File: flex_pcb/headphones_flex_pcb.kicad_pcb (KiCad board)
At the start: 2 copper layers, 41.7 x 25.7 mm, 15 parts, among them J1 LIGHTING_JACK, J2 CONN_01X01, J3 BOTTOM_FLEX_LIGHTNING, J5 LIGHTNING_HEADPHONE_ADAPTER, J7 IPHONE_HEADPHONE_JACK, U1 SN74LVC1G123, U2 SN74LVC1G123, U3 NC7S32-micropak6, U4 ADG774A-LFCSP

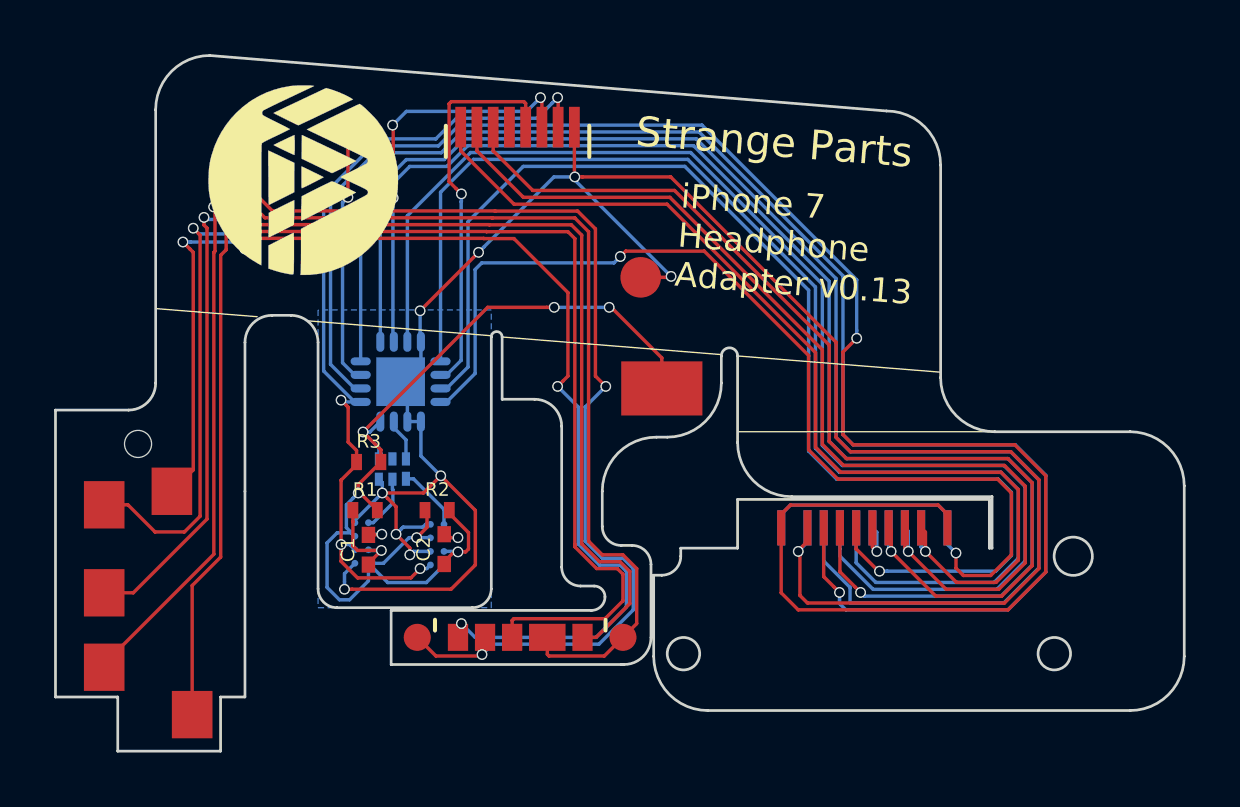
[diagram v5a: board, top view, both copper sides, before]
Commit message: Tweaks suggested by Lisa for manufacturability
- Change vias from 0.3/0.4 to 0.3/0.5
- Move tracks around lightning connector to at least 0.15mm away from board edge.
- Add silkscreen for all edge cuts (since they won’t cut for me)
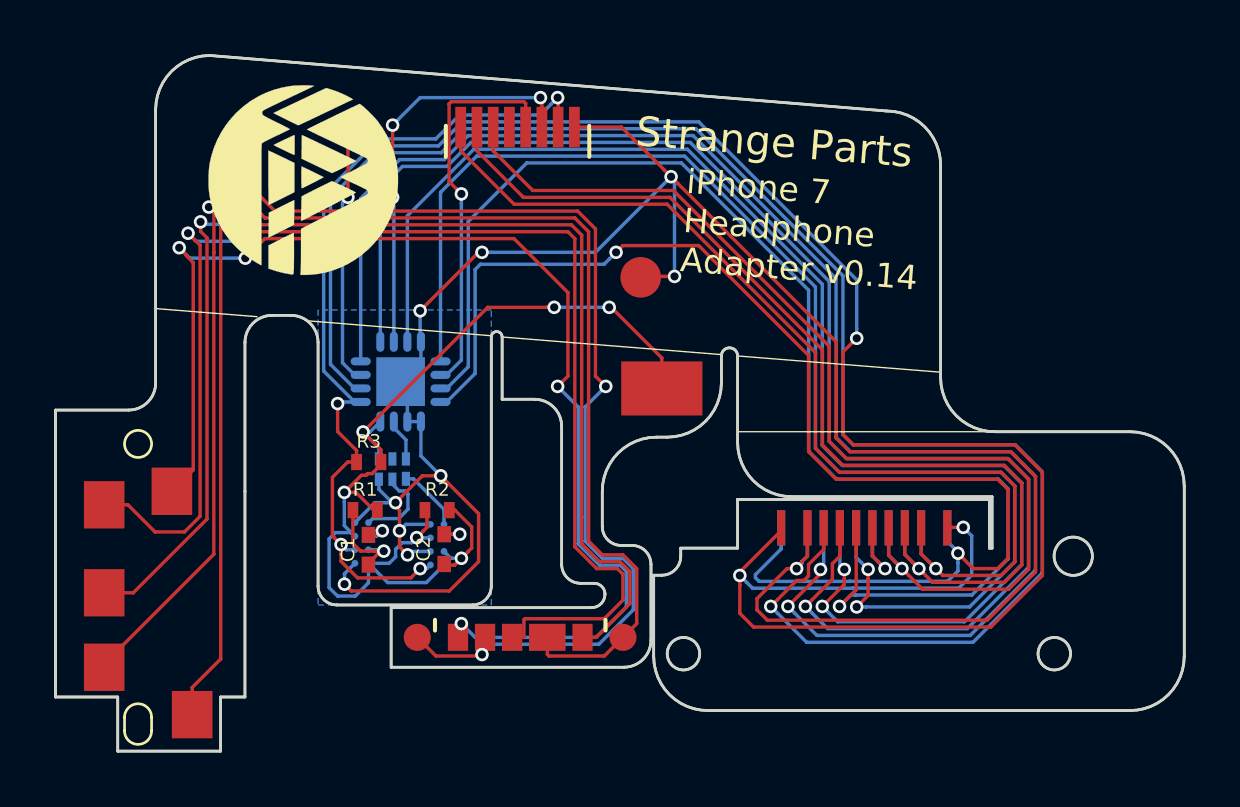
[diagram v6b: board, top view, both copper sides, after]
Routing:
- net /JSHIELD: track 81.0 -> 88.7 mm, vias 4 -> 6
- net GNDREF: track 85.6 -> 90.8 mm
- net /JPIN2: track 58.7 -> 62.9 mm
- net /JPIN3: track 51.5 -> 55.1 mm
- net /PPIN2: track 54.4 -> 58.1 mm, vias 0 -> 2
- net /JPIN4: track 45.5 -> 48.7 mm
- net /PPIN3: track 48.6 -> 51.8 mm, vias 0 -> 2
- net /PSHIELD: track 45.2 -> 47.9 mm
- net /PPIN4: track 47.1 -> 49.2 mm, vias 0 -> 2
- net /PPIN5: track 1.88 -> 3.40 mm
- net Net-(U1-Pad5): track 2.09 -> 3.13 mm
- net VCC: track 35.4 -> 36.2 mm
- net /PPIN6: track 39.2 -> 39.9 mm
- net /PPIN8: track 37.4 -> 38.0 mm
- net /PPIN7: track 38.3 -> 38.9 mm
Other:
- outline, holes or cut-outs redrawn
- net class Default: via_dia 0.4 -> 0.5
- rule via_min_size: 0.4 -> 0.5
- board text added: "iPhone 7 Headphone Adapter v0.14"
- board text removed: "iPhone 7 Headphone Adapter v0.13"

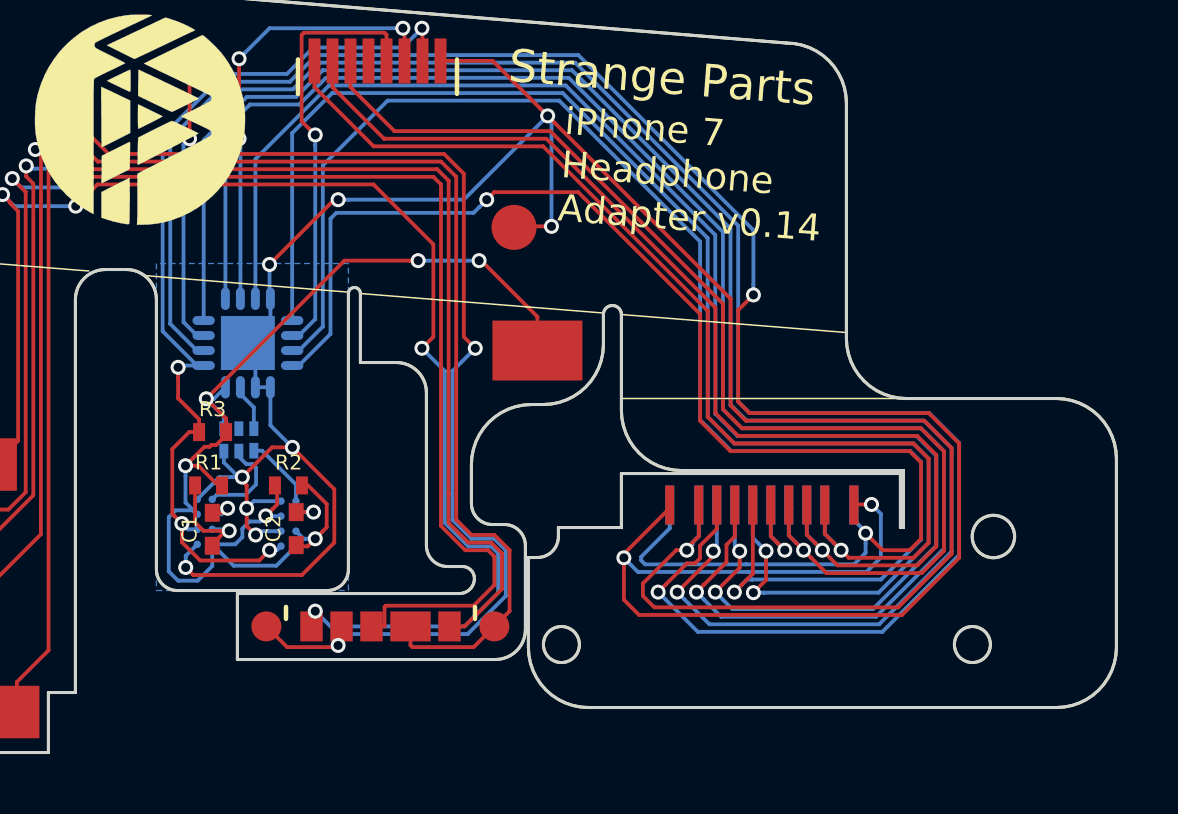
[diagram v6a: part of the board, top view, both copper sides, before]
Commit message: Tweaks to hopefully get rid of the large circles.
This seems to be only a problem on Lisa’s software.

Also add the holes for the lightning connector as actual drill holes in hopes they will drill them for me.
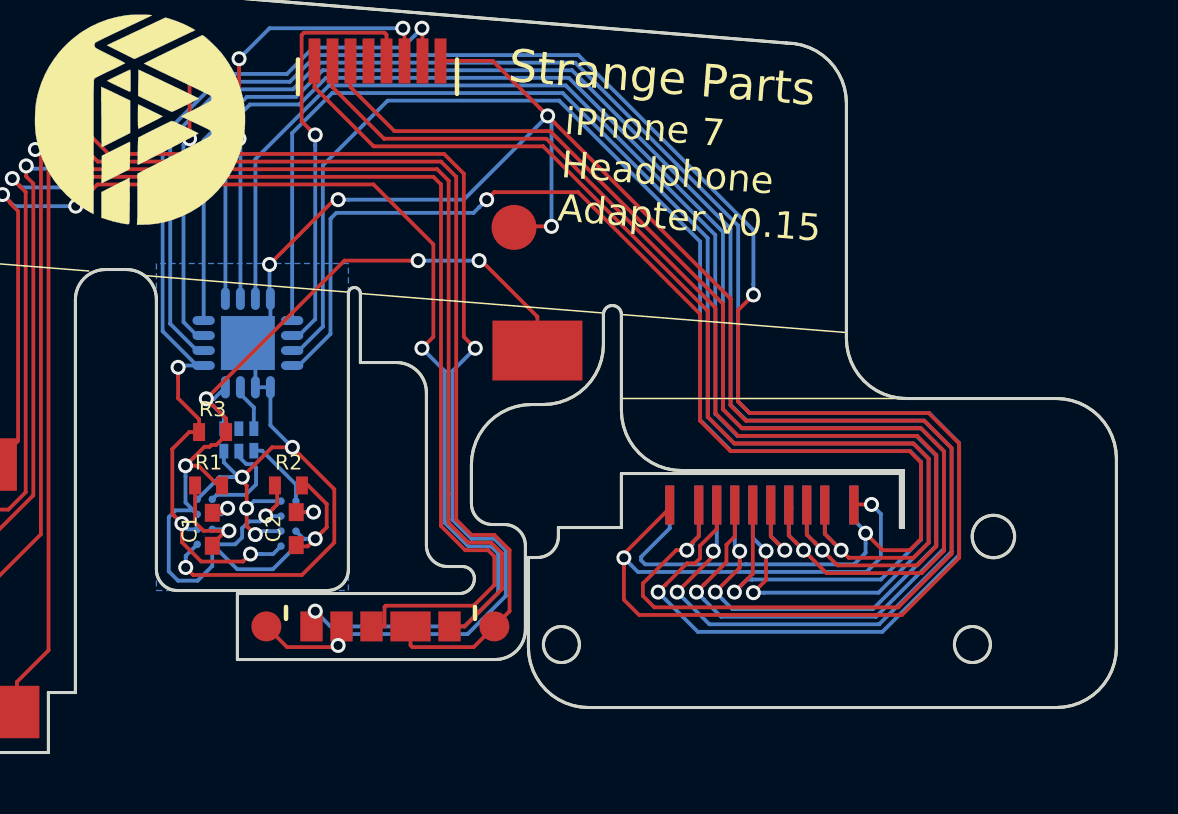
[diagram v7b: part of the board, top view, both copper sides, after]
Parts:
- added REF**: HOLE_1.2mm, holes:HOLE_1.2mm, F.Cu at (146.0, 82.9)
- added REF**: HOLE_1.2mm, holes:HOLE_1.2mm, F.Cu at (159.7, 82.9)
- added REF**: HOLE_1.4mm, holes:HOLE_1.4mm, F.Cu at (160.4, 79.3)
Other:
- board text added: "iPhone 7 Headphone Adapter v0.15"
- board text removed: "iPhone 7 Headphone Adapter v0.14"

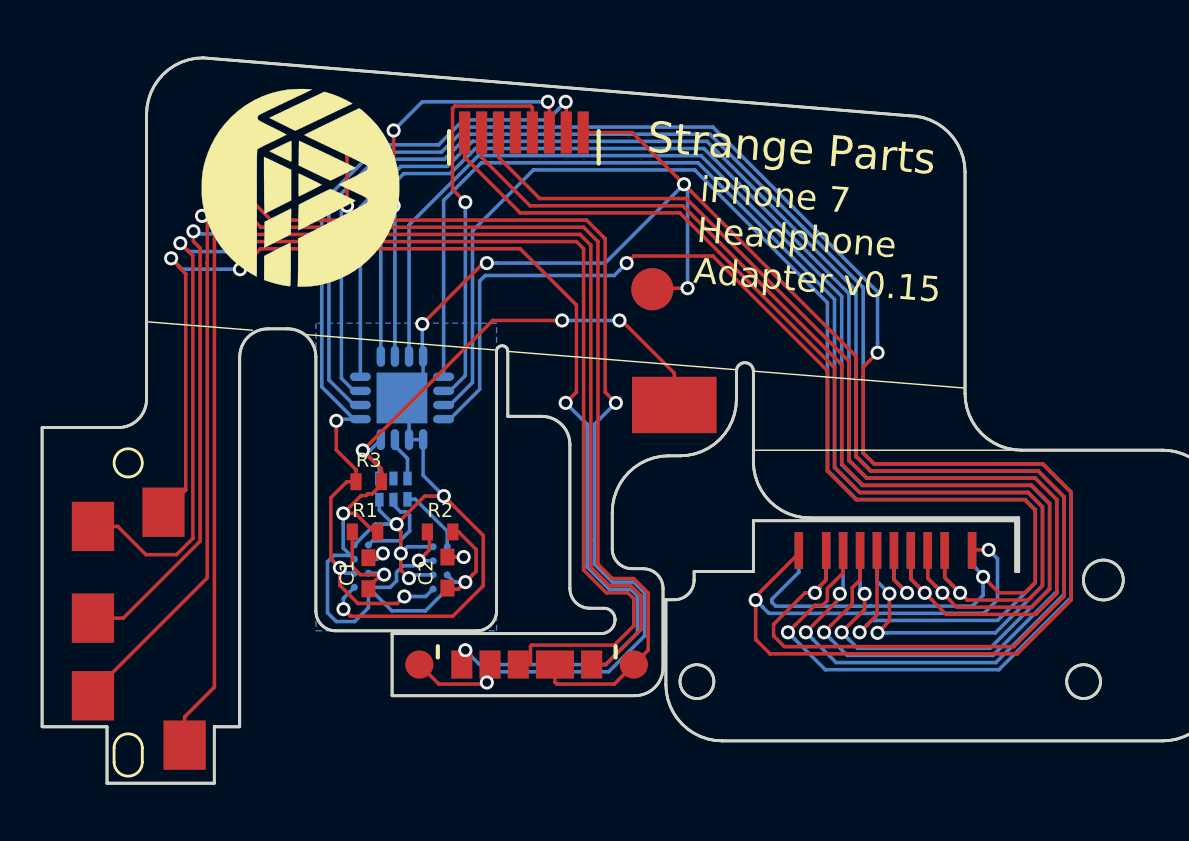
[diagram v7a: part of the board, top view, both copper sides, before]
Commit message: Move all the components to the bottom side
This is on Lisa’s recommendation.  She says because the FPC is so thin, it will be hard to solder if they’re on both sides.
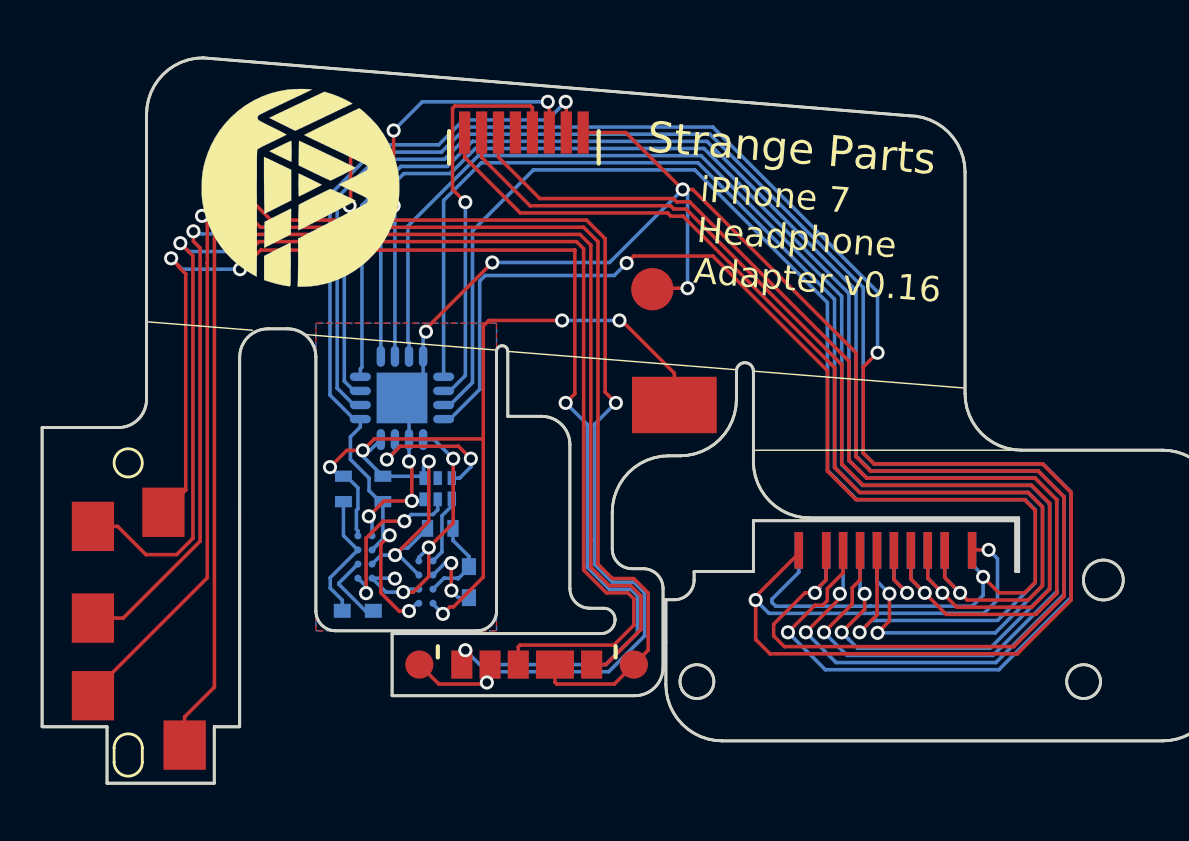
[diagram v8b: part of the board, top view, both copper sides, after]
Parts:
- C1, C2, R1, R2, R3: moved to B.Cu
- moved R1 1.70 mm to (133.5, 76.1), turned to 270 degrees
- moved U3 1.57 mm to (137.5, 75.6)
- moved C1 1.38 mm to (134.0, 80.4), turned to 0 degrees
- moved C2 0.83 mm to (137.9, 79.4), turned to 270 degrees
- moved U2 0.71 mm to (136.4, 79.4)
- moved R3 0.56 mm to (134.9, 76.1), turned to 270 degrees
- moved U1 0.35 mm to (134.2, 78.5), turned to 180 degrees
- moved R2 0.13 mm to (136.9, 77.5)
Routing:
- net GNDREF: track 90.8 -> 84.0 mm, vias 10 -> 12
- net VCC: track 36.3 -> 40.6 mm, vias 5 -> 7
- net Net-(U3-Pad4): track 1.56 -> 5.31 mm, vias 0 -> 2
- net Net-(U1-Pad5): track 3.13 -> 5.92 mm, vias 0 -> 2
- net /JSHIELD: track 88.7 -> 86.6 mm, vias 6 -> 5
- net Net-(C1-Pad2): track 1.18 -> 2.61 mm, vias 1 -> 0
- net Net-(C2-Pad2): track 1.26 -> 2.53 mm, vias 1 -> 2
- net Net-(J5-Pad15): track 45.8 -> 46.9 mm
- net Net-(C1-Pad1): track 3.93 -> 4.66 mm, vias 1 -> 0
- net Net-(C2-Pad1): track 3.82 -> 3.24 mm, vias 1 -> 0
- added copper zone on F.Cu, net GNDREF
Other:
- board text added: "iPhone 7 Headphone Adapter v0.16"
- board text removed: "iPhone 7 Headphone Adapter v0.15"
